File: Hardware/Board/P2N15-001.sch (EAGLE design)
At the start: 29 parts, among them IC1 TLC5941NT, IC2 LTC485N, IC3 74LS07N, IC4 LTC485N

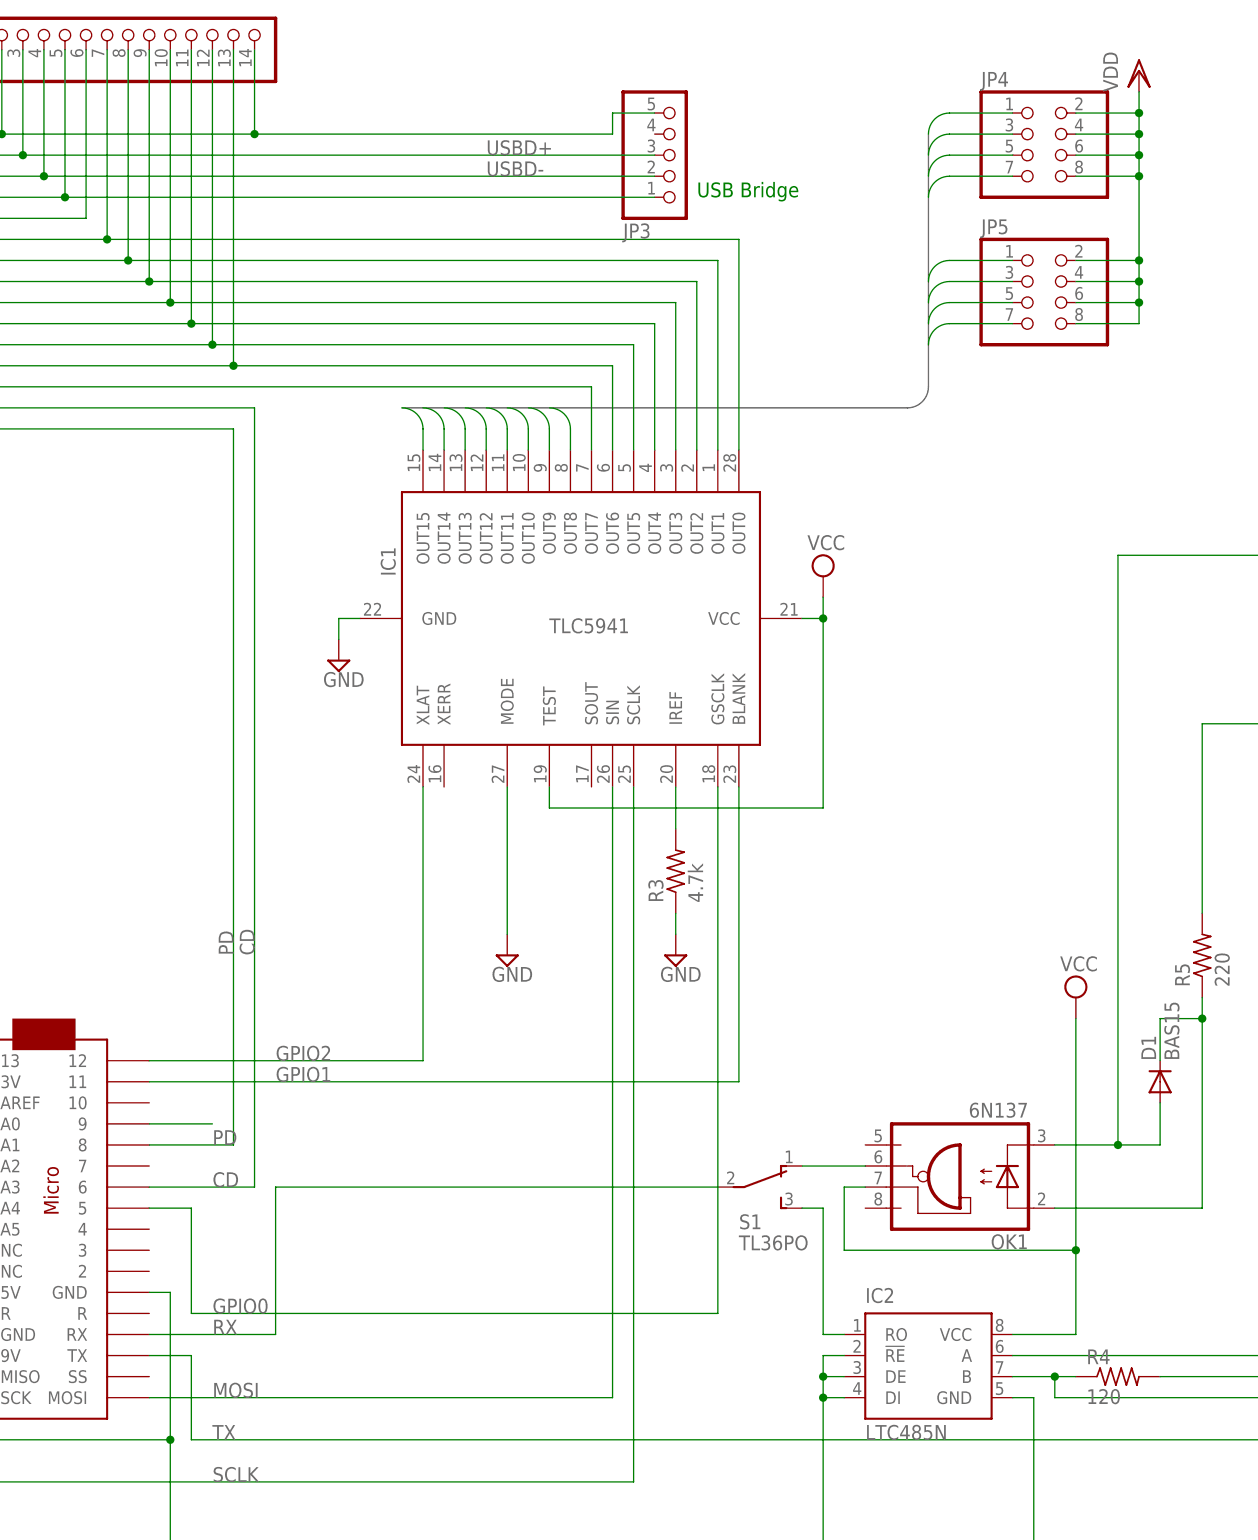
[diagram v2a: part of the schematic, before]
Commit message: Added Reset SW.
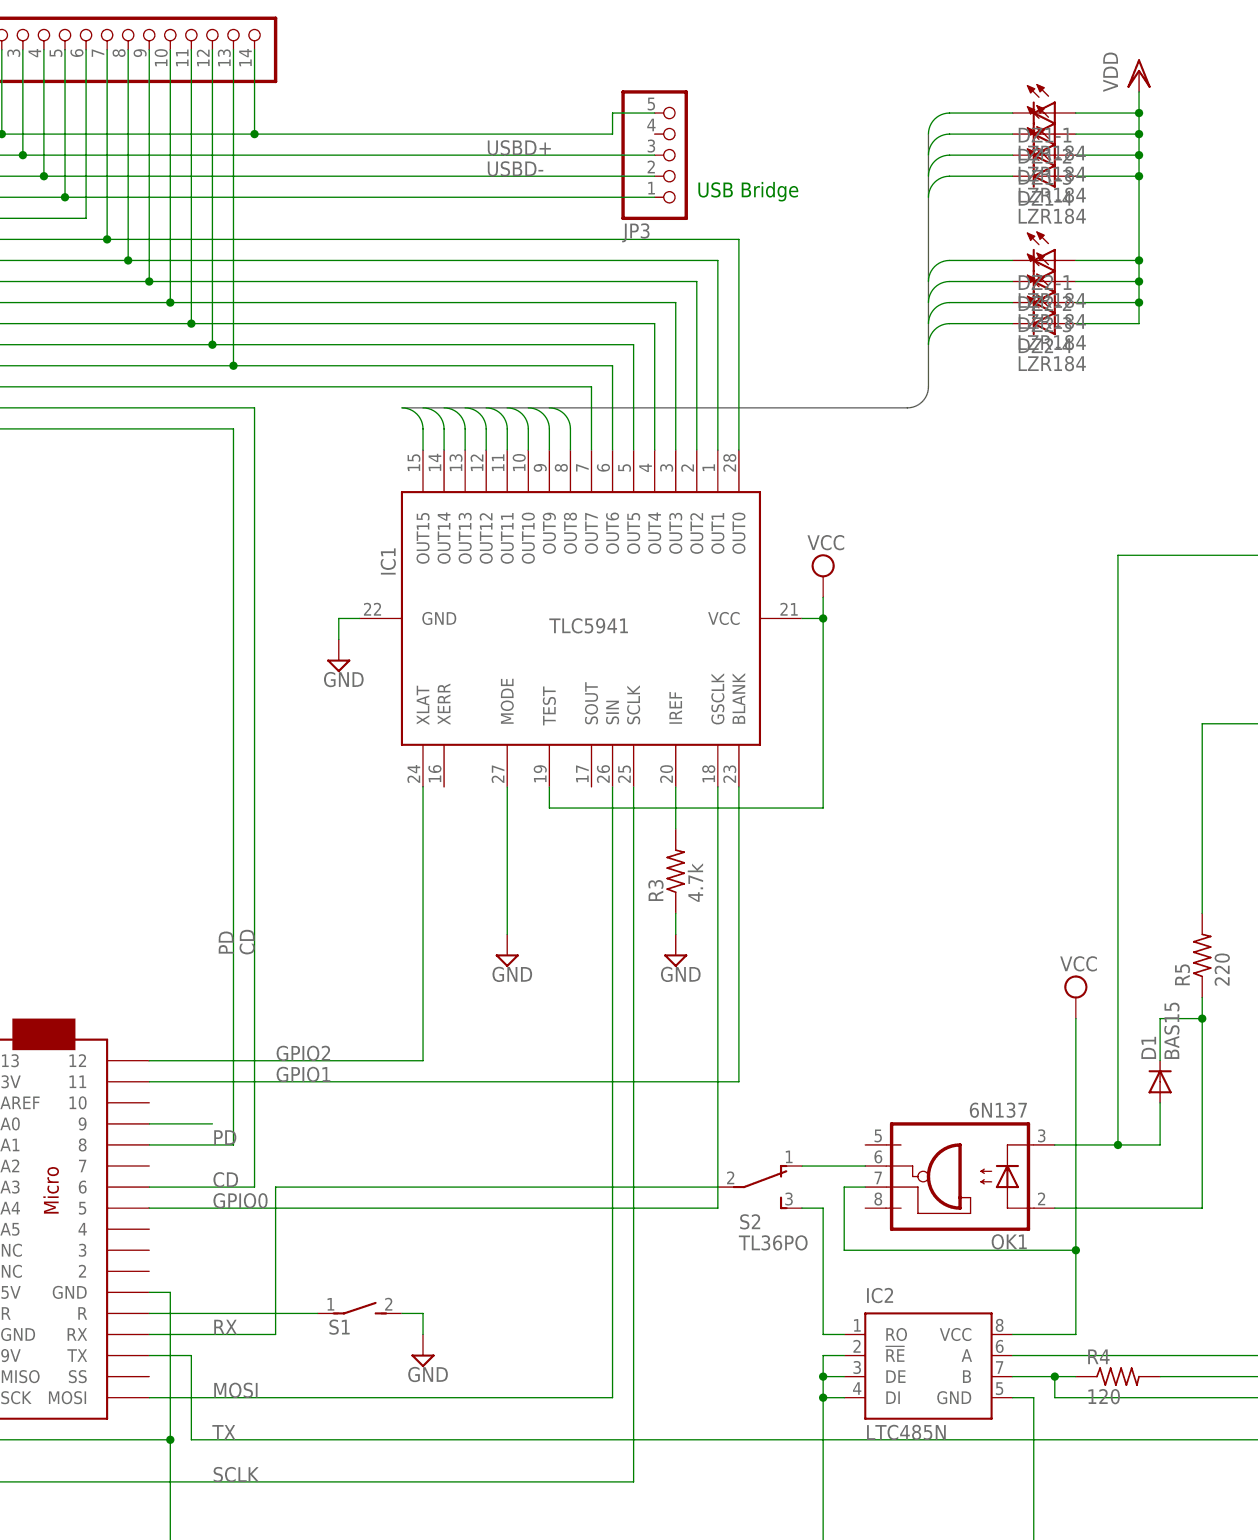
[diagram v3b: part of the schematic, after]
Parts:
- removed JP4, JP5: (no value), pinhead:PINHD-2X4
- added DZ1, DZ2: LZR184, led:LZR184
- added S2: TL36PO, switch:TL36PO
- S1: value TL36PO -> (none); device switch:TL36PO -> switch-dil:DS01E
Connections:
- new net N$5: MC1.R@2, S1.1
- net GND: now also S1.2
- net LED0: now also DZ1-1.C; no longer JP4.1
- net LED1: now also DZ1-2.C; no longer JP4.3
- net LED2: now also DZ1-3.C; no longer JP4.5
- net LED3: now also DZ1-4.C; no longer JP4.7
- net LED4: now also DZ2-1.C; no longer JP5.1
- net LED5: now also DZ2-2.C; no longer JP5.3
- net LED6: now also DZ2-3.C; no longer JP5.5
- net LED7: now also DZ2-4.C; no longer JP5.7
- net MIDIRX: now also S2.O; no longer S1.O
- net RX: now also S2.P; no longer S1.P
- net VDD: now also DZ1-1.A, DZ1-2.A, DZ1-3.A, DZ1-4.A, DZ2-1.A, DZ2-2.A, DZ2-3.A, DZ2-4.A; no longer JP4.2, JP4.4, JP4.6, JP4.8, JP5.2, JP5.4, JP5.6, JP5.8
- net XMIDIRX: now also S2.S; no longer S1.S

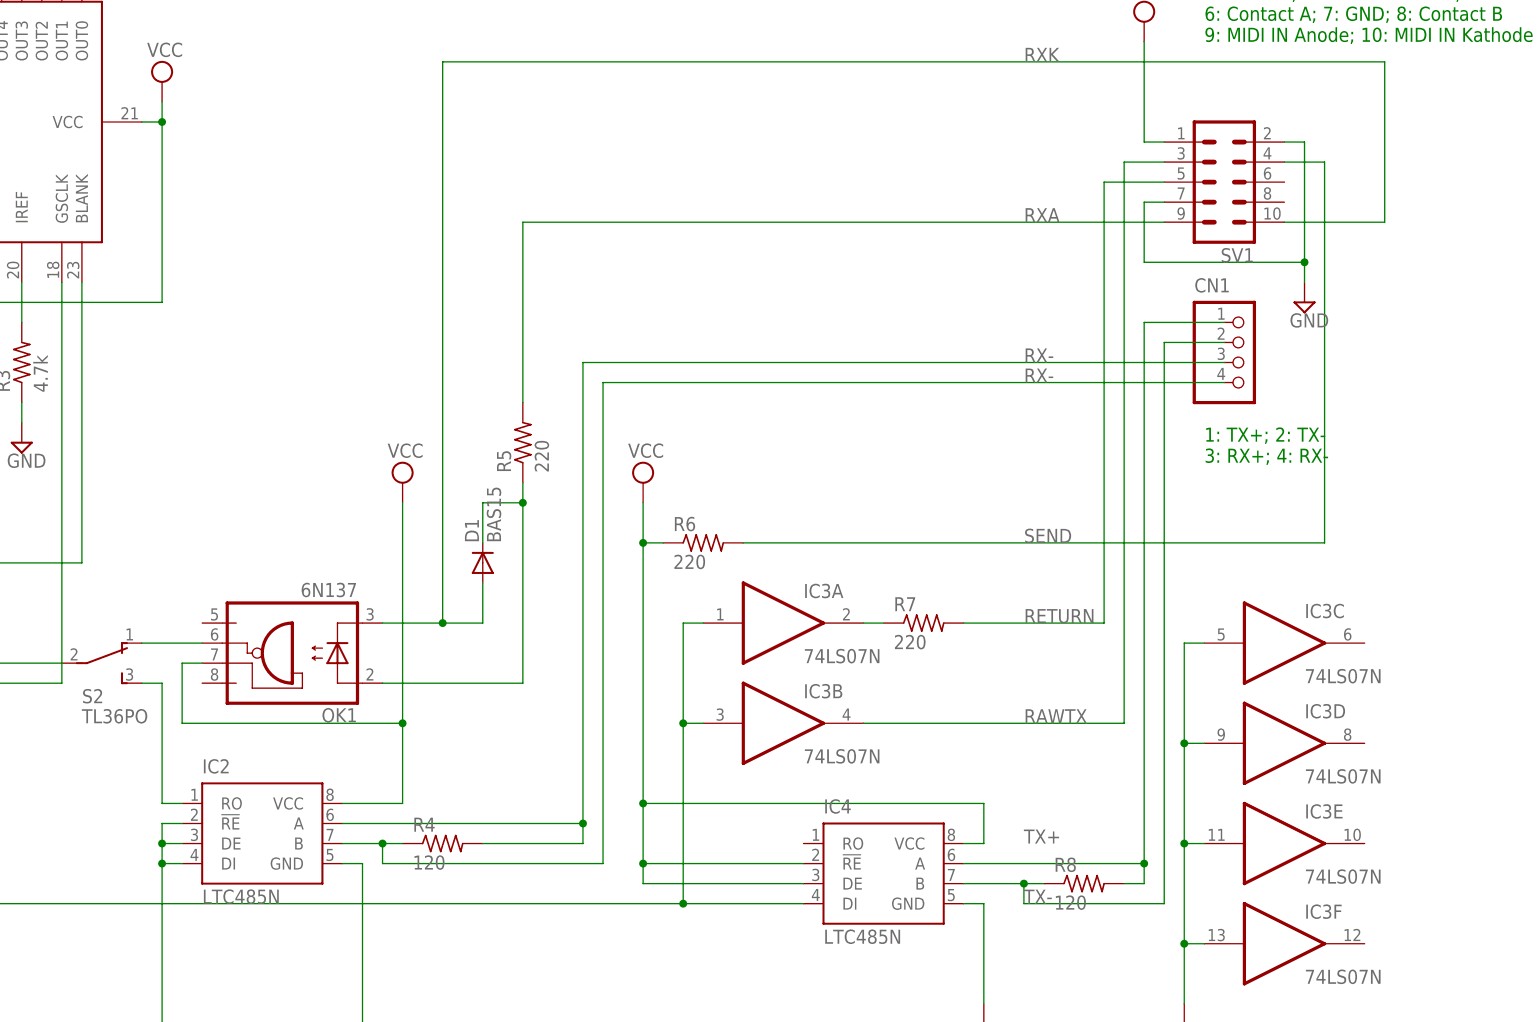
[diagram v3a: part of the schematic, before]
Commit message: Added MIDI THRU function.
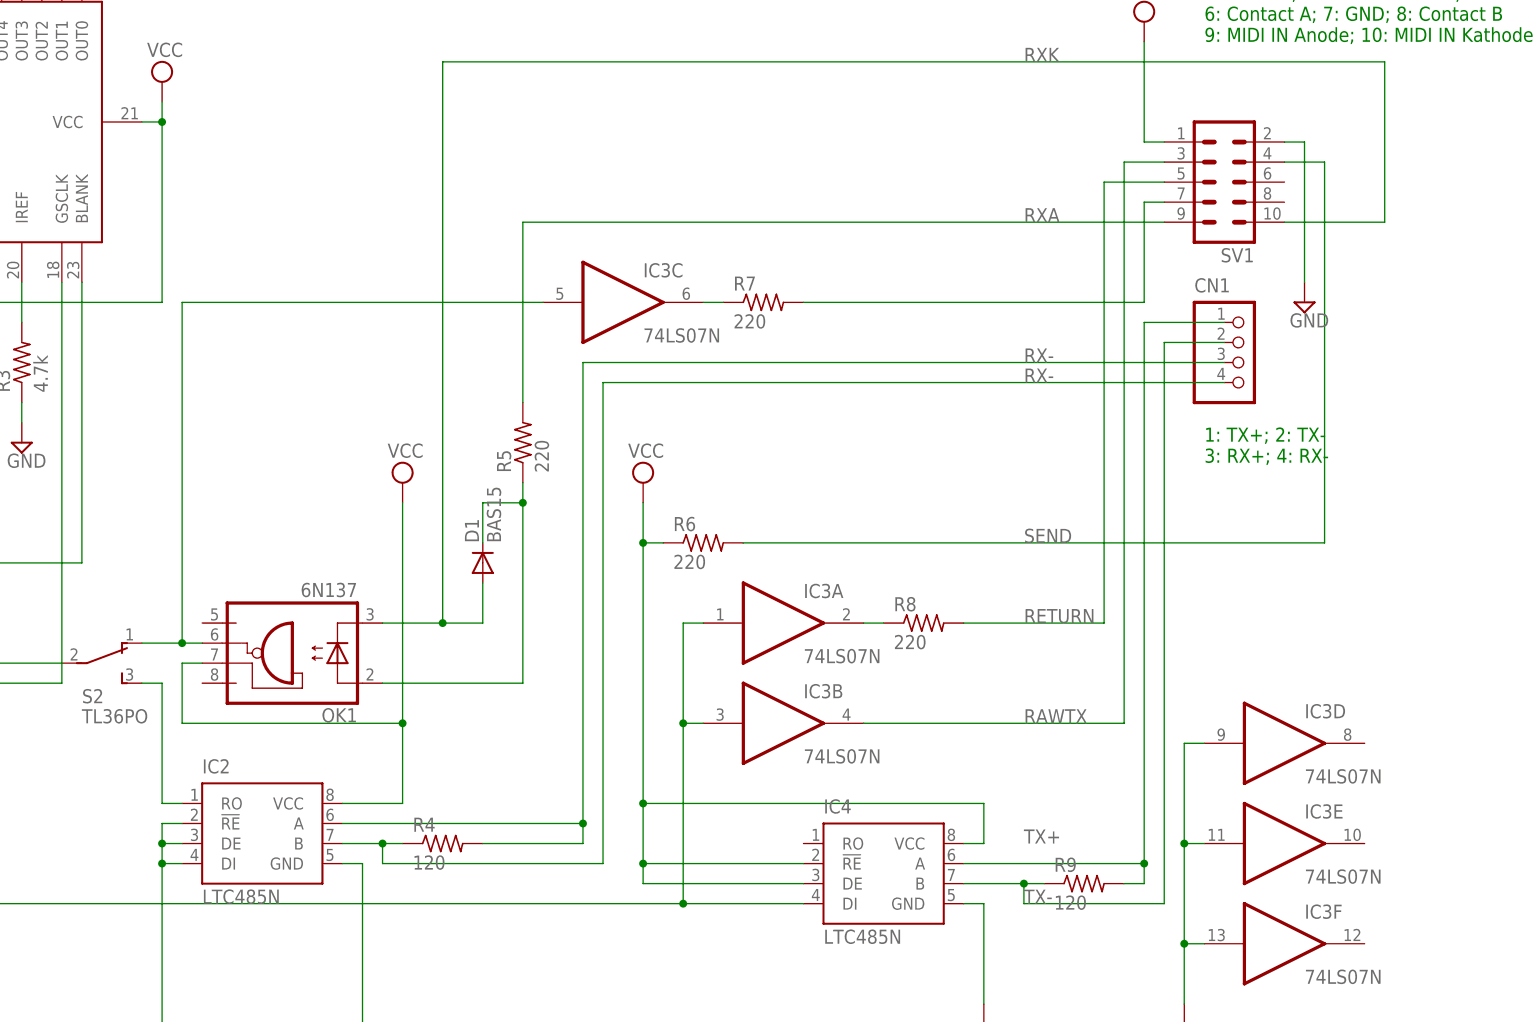
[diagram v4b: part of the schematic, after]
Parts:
- added R9: 120, resistor:R-US_0204/5
- R8: value 120 -> 220
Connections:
- new net N$6: IC3C.O, R7.1
- new net N$7: R7.2, SV1.7
- net GND: no longer IC3C.I, SV1.7
- net MIDIRX: now also IC3C.I
- net N$2: now also R8.1; no longer R7.1
- net RETURN: now also R8.2; no longer R7.2
- net TX+: now also R9.2; no longer R8.2
- net TX-: now also R9.1; no longer R8.1
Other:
- moved on the sheet: IC3C, R7, R8
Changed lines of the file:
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@@
 </classes>
 <parts>
-<part name="R7" library="resistor" deviceset="R-US_" device="0204/5" value="220"/>
+<part name="R8" library="resistor" deviceset="R-US_" device="0204/5" value="220"/>
 <part name="R5" library="resistor" deviceset="R-US_" device="0204/5" value="220"/>
 <part name="IC3" library="74xx-us" deviceset="74*07" device="N" technology="LS"/>
@@
 <part name="SUPPLY15" library="supply2" deviceset="GND" device=""/>
 <part name="R4" library="resistor" deviceset="R-US_" device="0204/5" value="120"/>
-<part name="R8" library="resistor" deviceset="R-US_" device="0204/5" value="120"/>
+<part name="R9" library="resistor" deviceset="R-US_" device="0204/5" value="120"/>
 <part name="SUPPLY18" library="supply2" deviceset="VCC" device=""/>
 <part name="SUPPLY21" library="supply2" deviceset="VCC" device=""/>
@@
 <part name="S1" library="switch-dil" deviceset="DS01E" device=""/>
 <part name="SUPPLY7" library="supply2" deviceset="GND" device=""/>
+<part name="R7" library="resistor" deviceset="R-US_" device="0204/5" value="220"/>
 </parts>
 <sheets>
@@
 </plain>
 <instances>
-<instance part="R7" gate="G$1" x="248.92" y="60.96"/>
+<instance part="R8" gate="G$1" x="248.92" y="60.96"/>
 <instance part="R5" gate="G$1" x="198.12" y="83.82" rot="R90"/>
 <instance part="IC3" gate="A" x="231.14" y="60.96"/>
@@
 <instance part="SUPPLY15" gate="GND" x="256.54" y="10.16"/>
 <instance part="R4" gate="G$1" x="187.96" y="33.02"/>
-<instance part="R8" gate="G$1" x="269.24" y="27.94"/>
+<instance part="R9" gate="G$1" x="269.24" y="27.94"/>
 <instance part="SUPPLY18" gate="G$1" x="271.78" y="180.34"/>
 <instance part="SUPPLY21" gate="G$1" x="279.4" y="180.34"/>
@@
 <instance part="MC1" gate="G$1" x="58.42" y="50.8" rot="R270"/>
 <instance part="IC3" gate="B" x="231.14" y="48.26"/>
-<instance part="IC3" gate="C" x="294.64" y="58.42"/>
+<instance part="IC3" gate="C" x="210.82" y="101.6"/>
 <instance part="VDD2" gate="G$1" x="7.62" y="40.64"/>
 <instance part="VDD3" gate="G$1" x="25.4" y="190.5"/>
@@
 <instance part="S1" gate="1" x="96.52" y="40.64" rot="R270"/>
 <instance part="SUPPLY7" gate="GND" x="104.14" y="35.56"/>
+<instance part="R7" gate="G$1" x="228.6" y="101.6"/>
 </instances>
 <busses>
@@
 <junction x="281.94" y="33.02"/>
 <junction x="281.94" y="20.32"/>
-<pinref part="IC3" gate="C" pin="I"/>
-<wire x1="284.48" y1="58.42" x2="281.94" y2="58.42" width="0.1524" layer="91"/>
-<wire x1="281.94" y1="58.42" x2="281.94" y2="45.72" width="0.1524" layer="91"/>
-<junction x="281.94" y="45.72"/>
 </segment>
 <segment>
@@
 <pinref part="SUPPLY28" gate="GND" pin="GND"/>
 <wire x1="294.64" y1="121.92" x2="297.18" y2="121.92" width="0.1524" layer="91"/>
-<wire x1="297.18" y1="121.92" x2="297.18" y2="106.68" width="0.1524" layer="91"/>
-<pinref part="SV1" gate="1" pin="7"/>
-<wire x1="297.18" y1="106.68" x2="297.18" y2="104.14" width="0.1524" layer="91"/>
-<wire x1="279.4" y1="114.3" x2="276.86" y2="114.3" width="0.1524" layer="91"/>
-<wire x1="276.86" y1="114.3" x2="276.86" y2="106.68" width="0.1524" layer="91"/>
-<wire x1="276.86" y1="106.68" x2="297.18" y2="106.68" width="0.1524" layer="91"/>
-<junction x="297.18" y="106.68"/>
+<wire x1="297.18" y1="121.92" x2="297.18" y2="104.14" width="0.1524" layer="91"/>
 </segment>
 <segment>
@@
 <segment>
 <pinref part="OK1" gate="A" pin="VO"/>
-<wire x1="149.86" y1="58.42" x2="157.48" y2="58.42" width="0.1524" layer="91"/>
+<wire x1="149.86" y1="58.42" x2="154.94" y2="58.42" width="0.1524" layer="91"/>
 <pinref part="S2" gate="BEF1" pin="O"/>
+<pinref part="IC3" gate="C" pin="I"/>
+<wire x1="154.94" y1="58.42" x2="157.48" y2="58.42" width="0.1524" layer="91"/>
+<wire x1="200.66" y1="101.6" x2="154.94" y2="101.6" width="0.1524" layer="91"/>
+<wire x1="154.94" y1="101.6" x2="154.94" y2="58.42" width="0.1524" layer="91"/>
+<junction x="154.94" y="58.42"/>
 </segment>
 </net>
@@
 <segment>
 <pinref part="IC3" gate="A" pin="O"/>
-<pinref part="R7" gate="G$1" pin="1"/>
+<pinref part="R8" gate="G$1" pin="1"/>
 <wire x1="241.3" y1="60.96" x2="243.84" y2="60.96" width="0.1524" layer="91"/>
 </segment>
@@
 <net name="TX+" class="0">
 <segment>
-<pinref part="R8" gate="G$1" pin="2"/>
+<pinref part="R9" gate="G$1" pin="2"/>
 <wire x1="276.86" y1="27.94" x2="274.32" y2="27.94" width="0.1524" layer="91"/>
 <pinref part="IC4" gate="G$1" pin="A"/>
@@
 <segment>
 <pinref part="IC4" gate="G$1" pin="B"/>
-<pinref part="R8" gate="G$1" pin="1"/>
+<pinref part="R9" gate="G$1" pin="1"/>
 <wire x1="254" y1="27.94" x2="261.62" y2="27.94" width="0.1524" layer="91"/>
 <pinref part="CN1" gate="G$1" pin="2"/>
@@
 <net name="RETURN" class="0">
 <segment>
-<pinref part="R7" gate="G$1" pin="2"/>
+<pinref part="R8" gate="G$1" pin="2"/>
 <wire x1="254" y1="60.96" x2="271.78" y2="60.96" width="0.1524" layer="91"/>
 <wire x1="271.78" y1="60.96" x2="271.78" y2="116.84" width="0.1524" layer="91"/>
@@
 </segment>
 </net>
+<net name="N$6" class="0">
+<segment>
+<pinref part="IC3" gate="C" pin="O"/>
+<pinref part="R7" gate="G$1" pin="1"/>
+<wire x1="223.52" y1="101.6" x2="220.98" y2="101.6" width="0.1524" layer="91"/>
+</segment>
+</net>
+<net name="N$7" class="0">
+<segment>
+<pinref part="SV1" gate="1" pin="7"/>
+<wire x1="279.4" y1="114.3" x2="276.86" y2="114.3" width="0.1524" layer="91"/>
+<wire x1="276.86" y1="114.3" x2="276.86" y2="101.6" width="0.1524" layer="91"/>
+<pinref part="R7" gate="G$1" pin="2"/>
+<wire x1="276.86" y1="101.6" x2="233.68" y2="101.6" width="0.1524" layer="91"/>
+</segment>
+</net>
